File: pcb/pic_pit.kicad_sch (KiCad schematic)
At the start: 19 parts, among them J15 PC SPK, J17 IOout, U10 8259A-2, U23 74LS573, U9 8254

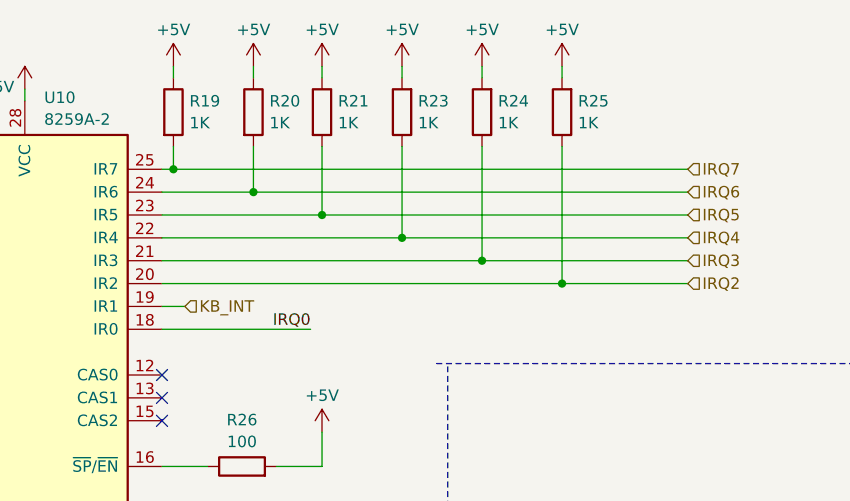
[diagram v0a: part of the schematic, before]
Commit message: 1052 vias down to 917, had to reshuffle some resistors and connectors
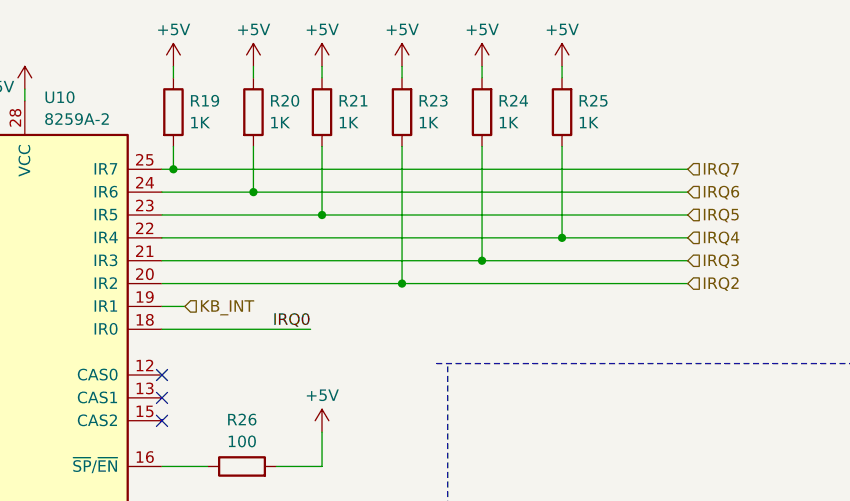
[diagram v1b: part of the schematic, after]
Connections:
- net IRQ2: now also R23.1; no longer R25.1
- net IRQ4: now also R25.1; no longer R23.1
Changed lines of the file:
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@@
 	)
 	(junction
-		(at 110.49 48.26)
+		(at 110.49 53.34)
+		(diameter 0)
+		(color 0 0 0 0)
+	)
+	(junction
+		(at 119.38 50.8)
+		(diameter 0)
+		(color 0 0 0 0)
+	)
+	(junction
+		(at 128.27 48.26)
 		(diameter 0)
 		(color 0 0 0 0)
@@
 		(color 0 0 0 0)
 	)
-	(junction
-		(at 128.27 53.34)
-		(diameter 0)
-		(color 0 0 0 0)
-	)
-	(junction
-		(at 119.38 50.8)
-		(diameter 0)
-		(color 0 0 0 0)
-	)
 	(no_connect
 		(at 83.82 68.58)
@@
 	(wire
 		(pts
-			(xy 128.27 53.34) (xy 128.27 38.1)
-		)
-		(stroke
-			(width 0)
-			(type default)
-		)
-	)
-	(wire
-		(pts
 			(xy 83.82 40.64) (xy 85.09 40.64)
 		)
@@
 	(wire
 		(pts
-			(xy 83.82 48.26) (xy 110.49 48.26)
-		)
-		(stroke
-			(width 0)
-			(type default)
-		)
-	)
-	(wire
-		(pts
 			(xy 80.01 161.29) (xy 82.55 161.29)
 		)
@@
 	(wire
 		(pts
+			(xy 224.79 100.33) (xy 220.98 100.33)
+		)
+		(stroke
+			(width 0)
+			(type default)
+		)
+	)
+	(wire
+		(pts
+			(xy 101.6 69.85) (xy 101.6 73.66)
+		)
+		(stroke
+			(width 0)
+			(type default)
+		)
+	)
+	(wire
+		(pts
+			(xy 104.14 160.02) (xy 104.14 158.75)
+		)
+		(stroke
+			(width 0)
+			(type default)
+		)
+	)
+	(wire
+		(pts
+			(xy 232.41 62.23) (xy 238.76 62.23)
+		)
+		(stroke
+			(width 0)
+			(type default)
+		)
+	)
+	(wire
+		(pts
+			(xy 85.09 29.21) (xy 85.09 30.48)
+		)
+		(stroke
+			(width 0)
+			(type default)
+		)
+	)
+	(wire
+		(pts
+			(xy 102.87 128.27) (xy 105.41 128.27)
+		)
+		(stroke
+			(width 0)
+			(type default)
+		)
+	)
+	(bus
+		(pts
+			(xy 184.15 100.33) (xy 184.15 97.79)
+		)
+		(stroke
+			(width 0)
+			(type default)
+		)
+	)
+	(bus
+		(pts
+			(xy 73.66 130.81) (xy 73.66 128.27)
+		)
+		(stroke
+			(width 0)
+			(type default)
+		)
+	)
+	(wire
+		(pts
 			(xy 83.82 50.8) (xy 119.38 50.8)
 		)
@@
 	(wire
 		(pts
-			(xy 224.79 100.33) (xy 220.98 100.33)
-		)
-		(stroke
-			(width 0)
-			(type default)
-		)
-	)
-	(wire
-		(pts
-			(xy 101.6 69.85) (xy 101.6 73.66)
-		)
-		(stroke
-			(width 0)
-			(type default)
-		)
-	)
-	(wire
-		(pts
-			(xy 104.14 160.02) (xy 104.14 158.75)
-		)
-		(stroke
-			(width 0)
-			(type default)
-		)
-	)
-	(wire
-		(pts
-			(xy 232.41 62.23) (xy 238.76 62.23)
-		)
-		(stroke
-			(width 0)
-			(type default)
-		)
-	)
-	(wire
-		(pts
-			(xy 85.09 29.21) (xy 85.09 30.48)
-		)
-		(stroke
-			(width 0)
-			(type default)
-		)
-	)
-	(wire
-		(pts
-			(xy 102.87 128.27) (xy 105.41 128.27)
-		)
-		(stroke
-			(width 0)
-			(type default)
-		)
-	)
-	(wire
-		(pts
-			(xy 128.27 53.34) (xy 142.24 53.34)
-		)
-		(stroke
-			(width 0)
-			(type default)
-		)
-	)
-	(bus
-		(pts
-			(xy 184.15 100.33) (xy 184.15 97.79)
-		)
-		(stroke
-			(width 0)
-			(type default)
-		)
-	)
-	(bus
-		(pts
-			(xy 73.66 130.81) (xy 73.66 128.27)
-		)
-		(stroke
-			(width 0)
-			(type default)
-		)
-	)
-	(wire
-		(pts
 			(xy 105.41 156.21) (xy 102.87 156.21)
 		)
@@
 		)
 	)
-	(wire
-		(pts
-			(xy 110.49 48.26) (xy 142.24 48.26)
-		)
-		(stroke
-			(width 0)
-			(type default)
-		)
-	)
 	(bus
 		(pts
@@
 	(wire
 		(pts
+			(xy 119.38 50.8) (xy 142.24 50.8)
+		)
+		(stroke
+			(width 0)
+			(type default)
+		)
+	)
+	(wire
+		(pts
 			(xy 101.6 30.48) (xy 101.6 29.21)
 		)
@@
 	(wire
 		(pts
+			(xy 110.49 53.34) (xy 142.24 53.34)
+		)
+		(stroke
+			(width 0)
+			(type default)
+		)
+	)
+	(wire
+		(pts
 			(xy 186.69 102.87) (xy 195.58 102.87)
 		)
@@
 	(wire
 		(pts
+			(xy 83.82 48.26) (xy 128.27 48.26)
+		)
+		(stroke
+			(width 0)
+			(type default)
+		)
+	)
+	(wire
+		(pts
 			(xy 210.82 38.1) (xy 222.25 38.1)
 		)
@@
 	(wire
 		(pts
-			(xy 83.82 53.34) (xy 128.27 53.34)
+			(xy 83.82 53.34) (xy 110.49 53.34)
 		)
 		(stroke
@@
 	(wire
 		(pts
+			(xy 128.27 48.26) (xy 142.24 48.26)
+		)
+		(stroke
+			(width 0)
+			(type default)
+		)
+	)
+	(wire
+		(pts
 			(xy 76.2 125.73) (xy 82.55 125.73)
 		)
@@
 	(wire
 		(pts
-			(xy 110.49 38.1) (xy 110.49 48.26)
+			(xy 110.49 38.1) (xy 110.49 53.34)
 		)
 		(stroke
@@
 		)
 	)
-	(wire
-		(pts
-			(xy 119.38 50.8) (xy 142.24 50.8)
-		)
-		(stroke
-			(width 0)
-			(type default)
-		)
-	)
 	(bus
 		(pts
@@
 	(wire
 		(pts
-			(xy 119.38 50.8) (xy 119.38 38.1)
+			(xy 119.38 38.1) (xy 119.38 50.8)
 		)
 		(stroke
@@
 		)
 		(stroke
+			(width 0)
+			(type default)
+		)
+	)
+	(wire
+		(pts
+			(xy 128.27 38.1) (xy 128.27 48.26)
+		)
+		(stroke
